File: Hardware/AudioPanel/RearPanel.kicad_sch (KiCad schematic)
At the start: 21 parts, among them J1 PWR IN, J12 COM Port, J13 COM Port, J14 COM Port, J15 COM Port, J16 USB_A, J17 MIC Port, J18 Speakers, J19 DATA Port, J21 MIC Port, J22 Speakers, J23 DATA Port, J25 GPS IN, J26 DATA Port, J29 MIC Port, J3 MIC Port, J30 Speakers, J31 DATA Port, J5 AudioJack2, J6 RCA x6, J8 RCA x6

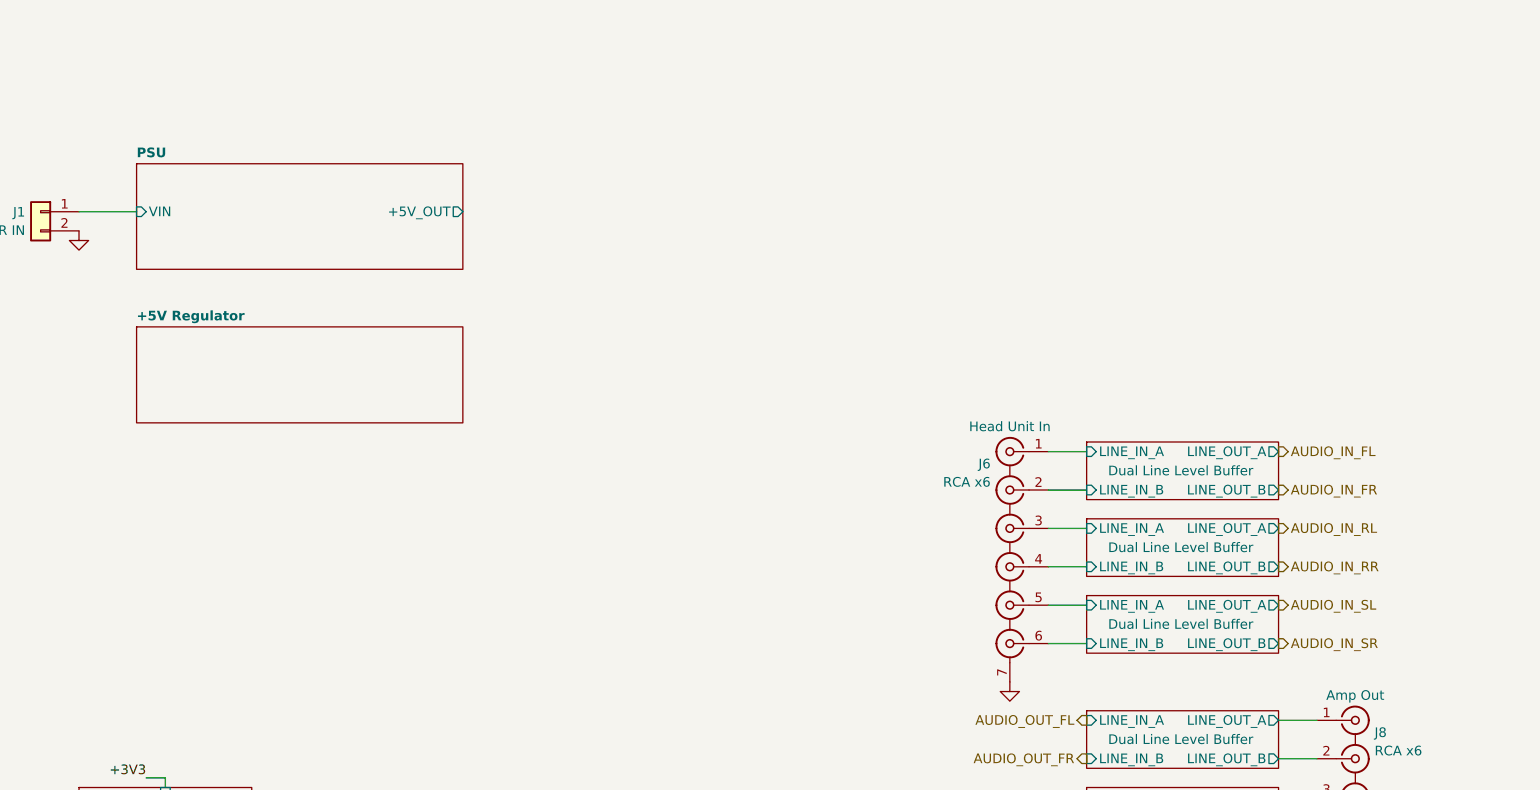
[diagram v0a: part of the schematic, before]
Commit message: Adding ADAV400 sheet
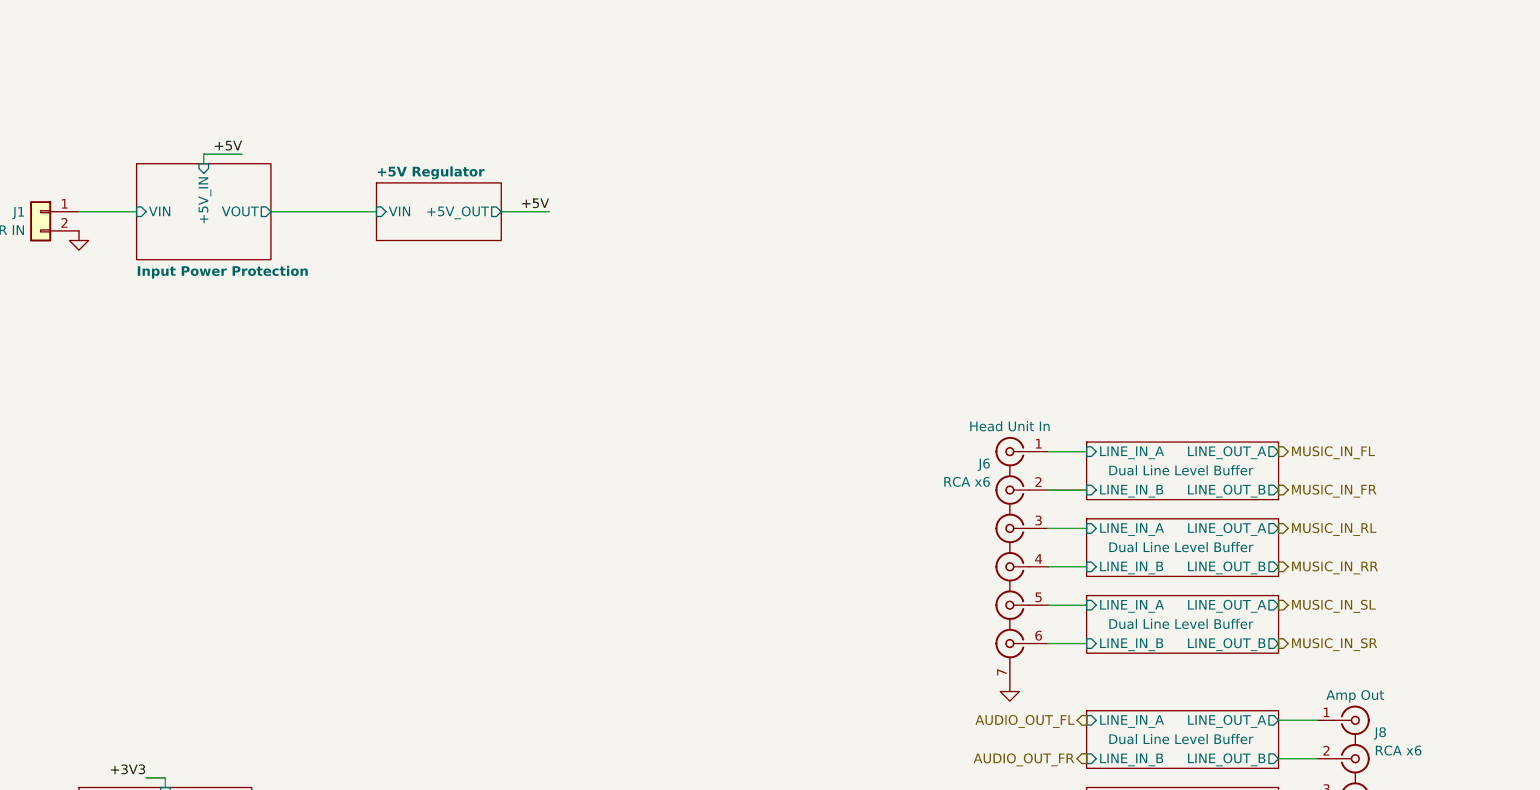
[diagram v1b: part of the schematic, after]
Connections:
- net Dual Line Level Buffer/LINE_IN_A is gone; now on net Dual Line Level Buffer/LINE_IN_A: J6.5 (IN2)
- net Dual Line Level Buffer/LINE_IN_B is gone; now on net Dual Line Level Buffer/LINE_IN_B: J6.6 (IN2)
- net Dual Line Level Buffer/LINE_OUT_A is gone; now on net Dual Line Level Buffer/LINE_OUT_A: J8.5 (IN2)
- net Dual Line Level Buffer/LINE_OUT_B is gone; now on net Dual Line Level Buffer/LINE_OUT_B: J8.6 (IN2)
- net Dual Line Level Buffer/LINE_IN_A: no longer J6.1 (IN1)
- net Dual Line Level Buffer/LINE_IN_B: no longer J6.2 (IN2)
- net Dual Line Level Buffer/LINE_OUT_A: no longer J8.1 (IN1)
- net Dual Line Level Buffer/LINE_OUT_B: no longer J8.2 (IN2)
- new net Dual Line Level Buffer/LINE_IN_A: J6.1 (IN1)
- new net Dual Line Level Buffer/LINE_IN_B: J6.2 (IN2)
- new net Dual Line Level Buffer/LINE_OUT_A: J8.1 (IN1)
- new net Dual Line Level Buffer/LINE_OUT_B: J8.2 (IN2)
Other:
- sheet PSU renamed Input Power Protection
- sheet +5V Regulator ports: added +5V_OUT, VIN; removed none
- sheet Input Power Protection ports: added +5V_IN, VOUT; removed +5V_OUT
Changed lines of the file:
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@@
 		)
 	)
+	(wire
+		(pts
+			(xy 162.56 161.29) (xy 176.53 161.29)
+		)
+		(stroke
+			(width 0)
+			(type default)
+		)
+	)
+	(wire
+		(pts
+			(xy 199.39 161.29) (xy 193.04 161.29)
+		)
+		(stroke
+			(width 0)
+			(type default)
+		)
+	)
 	(bus
 		(pts
@@
 	(wire
 		(pts
+			(xy 153.67 153.67) (xy 153.67 154.94)
+		)
+		(stroke
+			(width 0)
+			(type default)
+		)
+	)
+	(wire
+		(pts
 			(xy 309.88 115.57) (xy 327.66 115.57)
 		)
@@
 		)
 	)
+	(wire
+		(pts
+			(xy 158.75 153.67) (xy 153.67 153.67)
+		)
+		(stroke
+			(width 0)
+			(type default)
+		)
+	)
 	(bus
 		(pts
@@
 			"ADAATgBEAFMAQQBoAC8ARABYAFgANAA3AEQANABiAFMAMQB0AFgAMQA5AFAAegBRADAATgBEAFEA"
 			"MABOAEQAUQAwAE4ARABRADAATgBEAFQALwBUAGIANgBqAFEAbgA3ADAANgBOAEgAeQA1AGMAdQBY"
-			"AEwARgBtAEMAdwAwAHQAUwB1AEgASABqAGgAcg=="
+			"AEwARgBtAEMAdwAwAHQAUwB1AEgASABqAGgAcgByAGsAKwB2AHIANgAvAFAAeAA4AGMAMwBOAHoA"
+			"UABEAHoASQAwAHYASABtAHoAUgB2AEkAagB2AHMATgBpAFkAdQBMAG0AegBKAGwAQwBuAC8ANQA2"
+			"AE4ARwBqAG4AWgAyAGQAUgA0ADQAYwBhAFcAcABxAHkAdgA5AHUAYwAzAFAAegBpAFIATQBuAGMA"
+			"bgBOAHoAeQBVAFkAWgBDAEMARQAvAFAANwAvAFoAcwAyAGYAagBKAHAAQgBvAE4ARABjADMAOQA5"
+			"AHkANQBjADQANgBPAGoAdQBTAGEAWgBXAFYAbAA4AEUAMgBwAHEAYQBsAE4AbQB6AGEATgAvAEYA"
+			"WgBqAFkAKwBPAHAAVQA2AGMAUQBRAGgATQBtAFQATgBEAFgAMQB6ADkAegA1AGsAeAA5AGYAVAAx"
+			"AEMAYQBNAGEATQBHAGUAUwBzAEoARQBCAGEAVwB0AHIAegA1ADgAOABuAFQAWgBwAEUAeQBkAGcA"
+			"cABoAEkAYwBQAEgAegA1ADcAOQBnAHcAaABOAEgAVABvAFUAQQBzAEwAQwA0AEYAMQBjAG4ATgB6"
+			"ADcAOQAyADcAaAB4AEEAeQBOAGoAYQBHAEIASwBFAEkAbwBXAHYAWAByAGgAVQBWAEYAZgBGAFgA"
+			"MQB0AEQAUQBjAEgAQgB3ADYATwBiAFYAYQBXAGgAbwBhAEcAaABvAGEARwBoAG8ALwBvAFYAMABK"
+			"ADIAbAB5AGMASABBAHcAUQBvAGoAQgBZAFAAagA3ACsAKwBOAEMAVgAxAGYAWAB3AFkATQBIAEQA"
+			"eAA0ADgAKwBOAHkANQBjADcAagB3ACsAUABIAGoAVQBCAGcAVQBGAE8AVABrADUAQQBSAC8ANQAr"
+			"AFQAawA3AE4AeQA1AEUAMAA2AFMARQBVAEoASwBTAGsAcQAyAHQAcgBhAGwAcABhAFYAWAByADEA"
+			"NgBGAEUAawBkAEgAeAA0AGMAUABIADAASgBsAFMAMAB2AEwAegBNAHoATQBwAHEAYQBtAHIAZwBh"
+			"AFQAbABaAFcARgBGADkAQwB6AFoAcwAzAEsAegBNAHkAcwByAEsAdwA4AGMAdQBRAEkAbABNAHkA"
+			"WgBNADQAYwBnAGkATwBMAGkANABzAHgATwB1AEYAegB1AEYAKwBTAEoALwBpAFoAOAArAFAAQQBo"
+			"AEkAeQBPAGoAcwBiAEgAeABSAHcAMABBAEUAeABVAFYAQgBiAGsATgBsAHkANQBkACsAcQBQAEgA"
+			"MABsADMATwBuAHoAOABQADMANgBtADcAdQB6AHUANQBmAE8ALwBlAHYAWABqADIAMgB0AHYAYgBr"
+			"ADkAKwA2AGQAZQBzAFcAYQBHAGsANwBPAHoAdQ=="
 		)
 	)
@@
 		)
 	)
+	(label "+5V"
+		(at 158.75 153.67 180)
+		(effects
+			(font
+				(size 1.27 1.27)
+			)
+			(justify right bottom)
+		)
+	)
 	(label "700_DATA.1200RX"
 		(at 392.43 57.15 0)
@@
 		)
 	)
+	(label "+5V"
+		(at 199.39 161.29 180)
+		(effects
+			(font
+				(size 1.27 1.27)
+			)
+			(justify right bottom)
+		)
+	)
 	(label "D700_DATA_SQC"
 		(at 309.88 62.23 0)
@@
 		)
 	)
-	(hierarchical_label "AUDIO_IN_SR"
+	(hierarchical_label "MUSIC_IN_SR"
 		(shape output)
 		(at 295.91 218.44 0)
@@
 		)
 	)
-	(hierarchical_label "AUDIO_IN_FR"
+	(hierarchical_label "MUSIC_IN_FR"
 		(shape output)
 		(at 295.91 198.12 0)
@@
 		)
 	)
-	(hierarchical_label "AUDIO_IN_FL"
+	(hierarchical_label "MUSIC_IN_FL"
 		(shape output)
 		(at 295.91 193.04 0)
@@
 		)
 	)
-	(hierarchical_label "AUDIO_IN_RR"
+	(hierarchical_label "MUSIC_IN_RR"
 		(shape output)
 		(at 295.91 208.28 0)
@@
 		)
 	)
-	(hierarchical_label "AUDIO_IN_RL"
+	(hierarchical_label "MUSIC_IN_RL"
 		(shape output)
 		(at 295.91 203.2 0)
@@
 		)
 	)
-	(hierarchical_label "AUDIO_IN_SL"
+	(hierarchical_label "MUSIC_IN_SL"
 		(shape output)
 		(at 295.91 213.36 0)
@@
 	)
 	(sheet
-		(at 144.78 176.53)
-		(size 43.18 12.7)
+		(at 176.53 157.48)
+		(size 16.51 7.62)
 		(exclude_from_sim no)
 		(in_bom yes)
@@
 		)
 		(property "Sheetname" "+5V Regulator"
-			(at 144.78 175.8184 0)
+			(at 176.53 156.7684 0)
 			(effects
 				(font
@@
 		)
 		(property "Sheetfile" "PSU_5V.kicad_sch"
-			(at 144.78 189.8146 0)
+			(at 176.53 165.6846 0)
 			(effects
 				(font
@@
 			)
 		)
+		(pin "+5V_OUT" output
+			(at 193.04 161.29 0)
+			(effects
+				(font
+					(size 1.27 1.27)
+				)
+				(justify right)
+			)
+		)
+		(pin "VIN" input
+			(at 176.53 161.29 180)
+			(effects
+				(font
+					(size 1.27 1.27)
+				)
+				(justify left)
+			)
+		)
 		(instances
 			(project "PilotAudioPanel"
@@
 	(sheet
 		(at 144.78 154.94)
-		(size 43.18 13.97)
+		(size 17.78 12.7)
 		(exclude_from_sim no)
 		(in_bom yes)
 		(on_board yes)
 		(dnp no)
-		(fields_autoplaced yes)
 		(stroke
 			(width 0.1524)
@@
 			(color 128 255 128 1.0000)
 		)
-		(property "Sheetname" "PSU"
-			(at 144.78 154.2284 0)
+		(property "Sheetname" "Input Power Protection"
+			(at 144.78 169.926 0)
 			(effects
 				(font
@@
 		)
 		(property "Sheetfile" "PWR_IN.kicad_sch"
-			(at 144.78 169.4946 0)
+			(at 144.78 168.2246 0)
 			(effects
 				(font
@@
 			)
 		)
-		(pin "+5V_OUT" output
-			(at 187.96 161.29 0)
+		(pin "+5V_IN" input
+			(at 153.67 154.94 90)
+			(effects
+				(font
+					(size 1.27 1.27)
+				)
+				(justify right)
+			)
+		)
+		(pin "VOUT" output
+			(at 162.56 161.29 0)
 			(effects
 				(font

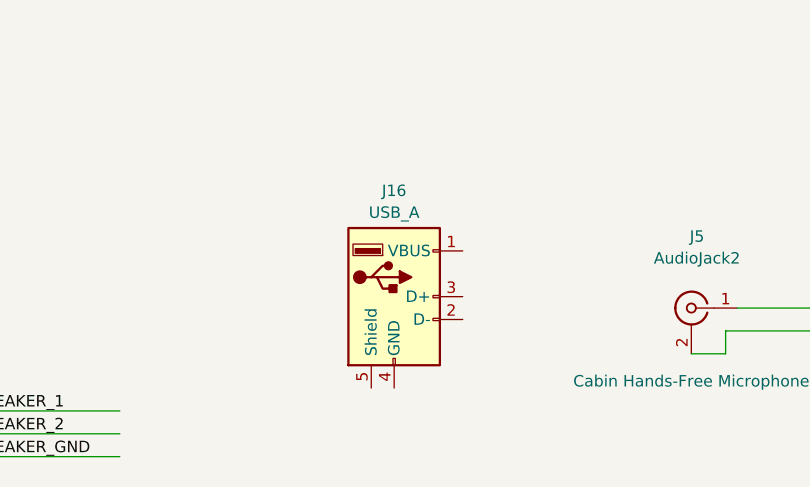
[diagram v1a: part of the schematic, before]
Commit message: Added USB hub, completed ADAV400 sheet, working on USBi programmer connections
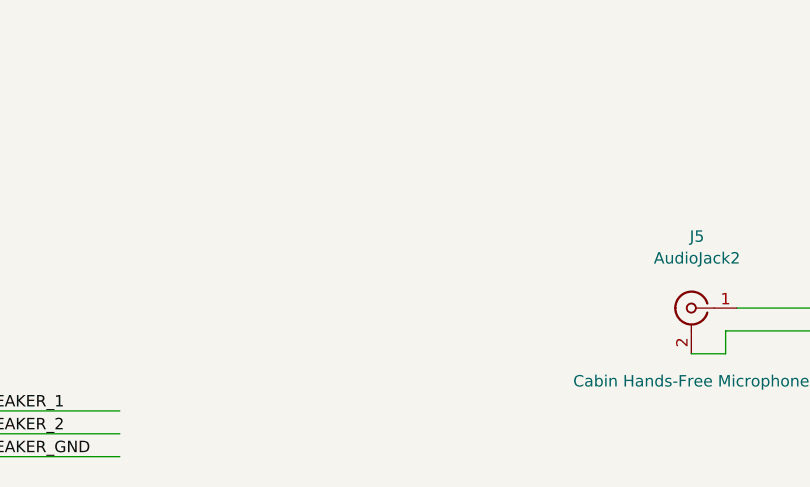
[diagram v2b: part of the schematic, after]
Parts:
- removed J16: USB_A, symbol Connector:USB_A
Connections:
- net Dual Line Level Buffer/LINE_IN_A is gone; now on net Dual Line Level Buffer/LINE_IN_A: J6.5 (IN2)
- net Dual Line Level Buffer/LINE_IN_B is gone; now on net Dual Line Level Buffer/LINE_IN_B: J6.6 (IN2)
- net Dual Line Level Buffer/LINE_OUT_A is gone; now on net Dual Line Level Buffer/LINE_OUT_A: J8.5 (IN2)
- net Dual Line Level Buffer/LINE_OUT_B is gone; now on net Dual Line Level Buffer/LINE_OUT_B: J8.6 (IN2)
- net Dual Line Level Buffer/LINE_IN_A: no longer J6.1 (IN1)
- net Dual Line Level Buffer/LINE_IN_B: no longer J6.2 (IN2)
- net Dual Line Level Buffer/LINE_OUT_A: no longer J8.1 (IN1)
- net Dual Line Level Buffer/LINE_OUT_B: no longer J8.2 (IN2)
- new net Dual Line Level Buffer/LINE_IN_A: J6.1 (IN1)
- new net Dual Line Level Buffer/LINE_IN_B: J6.2 (IN2)
- new net Dual Line Level Buffer/LINE_OUT_A: J8.1 (IN1)
- new net Dual Line Level Buffer/LINE_OUT_B: J8.2 (IN2)
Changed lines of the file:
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@@
-	)
-	(symbol
-		(lib_id "Connector:USB_A")
-		(at 83.82 243.84 0)
-		(unit 1)
-		(exclude_from_sim no)
-		(in_bom yes)
-		(on_board yes)
-		(dnp no)
-		(fields_autoplaced yes)
-		(property "Reference" "J16"
-			(at 83.82 232.0755 0)
-			(effects
-				(font
-					(size 1.27 1.27)
-				)
-			)
-		)
-		(property "Value" "USB_A"
-			(at 83.82 234.4998 0)
-			(effects
-				(font
-					(size 1.27 1.27)
-				)
-			)
-		)
-		(property "Footprint" ""
-			(at 87.63 245.11 0)
-			(effects
-				(font
-					(size 1.27 1.27)
-				)
-				(hide yes)
-			)
-		)
-		(property "Datasheet" "~"
-			(at 87.63 245.11 0)
-			(effects
-				(font
-					(size 1.27 1.27)
-				)
-				(hide yes)
-			)
-		)
-		(property "Description" "USB Type A connector"
-			(at 83.82 243.84 0)
-			(effects
-				(font
-					(size 1.27 1.27)
-				)
-				(hide yes)
-			)
-		)
-		(pin "5"
-		)
-		(pin "4"
-		)
-		(pin "1"
-		)
-		(pin "3"
-		)
-		(pin "2"
-		)
-		(instances
-			(project "PilotAudioPanel"
-				(path "/2de36a1b-eee5-458c-8325-256a7162eff5/f62958c9-d11c-4e53-b6fe-8fb24d1ad04a"
-					(reference "J16")
-					(unit 1)
-				)
-			)
-		)
 	)
 	(symbol
